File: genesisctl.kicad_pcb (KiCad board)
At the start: 2 copper layers, 12 parts, among them J1 Conn_02x05_Odd_Even, J2 Screw_Terminal_01x02, J3 Screw_Terminal_01x04, J4 Screw_Terminal_01x04, U1 NE555, U2 74LS374, U3 74LS74, U4 74LS374

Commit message: added gerber files
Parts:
- C1, C2: value 3.3uF -> 0.22uF
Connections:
- U4 pad 2: /left_out -> /right_out
- U4 pad 3: /gnd_left -> /gnd_right
- U4 pad 4: /gnd_right -> /gnd_left
- U4 pad 5: /right_out -> /left_out
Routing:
- net /select: track 0.00 -> 90.6 mm
- net /btna_out: track 0.00 -> 51.9 mm
- net Net-(U2-Pad11): track 0.00 -> 42.5 mm
- net /start_btnc: track 0.00 -> 34.0 mm
- net /right_out: track 0.00 -> 31.7 mm
- net /btna_btnb: track 0.00 -> 31.4 mm
- net btnb_out: track 0.00 -> 31.3 mm
- net Net-(C2-Pad1): track 0.00 -> 27.6 mm
- net /down: track 0.00 -> 26.3 mm
- net /up: track 0.00 -> 26.2 mm
- net btnc_out: track 0.00 -> 23.6 mm
- net /left_out: track 0.00 -> 23.2 mm
- net /start_out: track 0.00 -> 21.5 mm
- net GND: track 0.00 -> 17.7 mm, vias 0 -> 4
- net Net-(C1-Pad1): track 0.00 -> 16.1 mm
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- added copper zone on B.Cu, net +5V
- added copper zone on F.Cu, net GND
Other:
- board outline added: 48.3 x 63.5 mm
- board text added: "+5V"
- board text added: "A"
- board text added: "B"
- board text added: "C"
- board text added: "Down"
- board text added: "GND"
- board text added: "Genesis Jamma v1.0 2021 Sean Kasun"
- board text added: "Left"
- board text added: "Pin1"
- board text added: "Right"
- board text added: "Start"
- board text added: "Up"

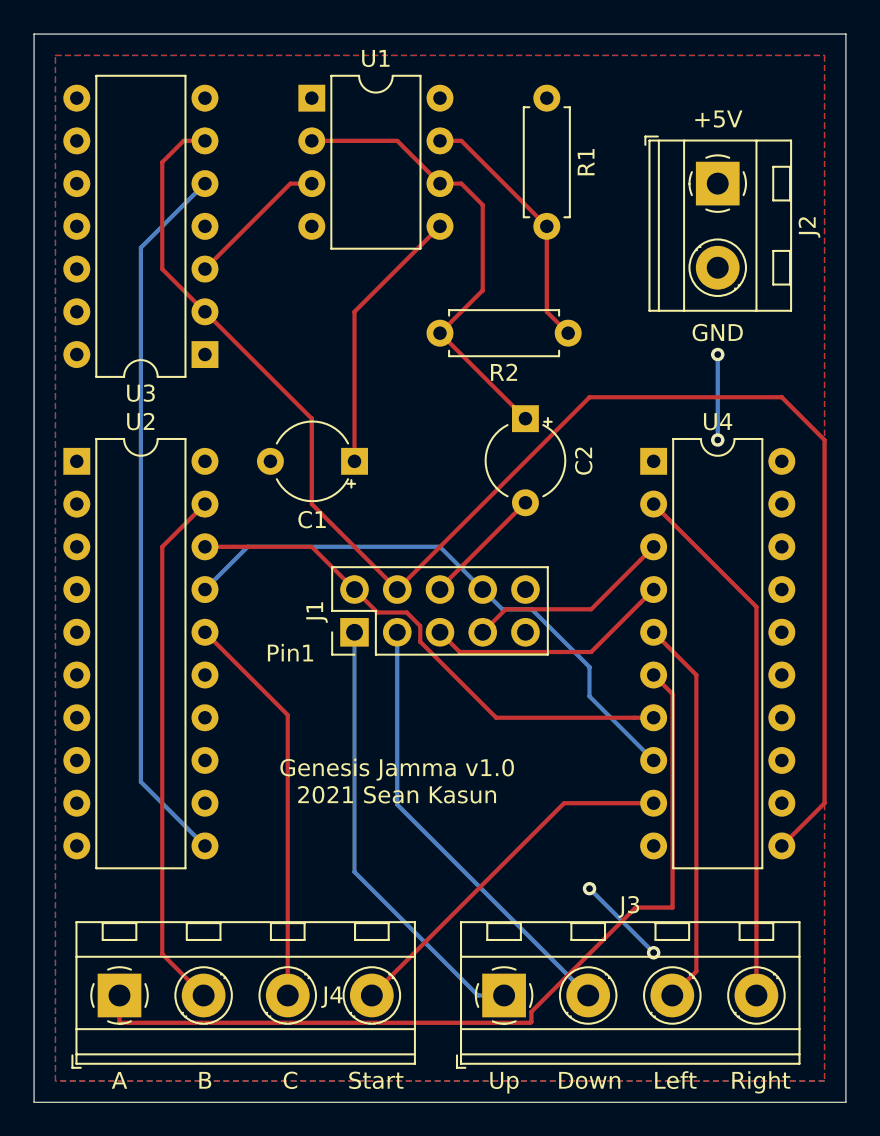
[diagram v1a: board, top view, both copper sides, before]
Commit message: fixed reversed left/right
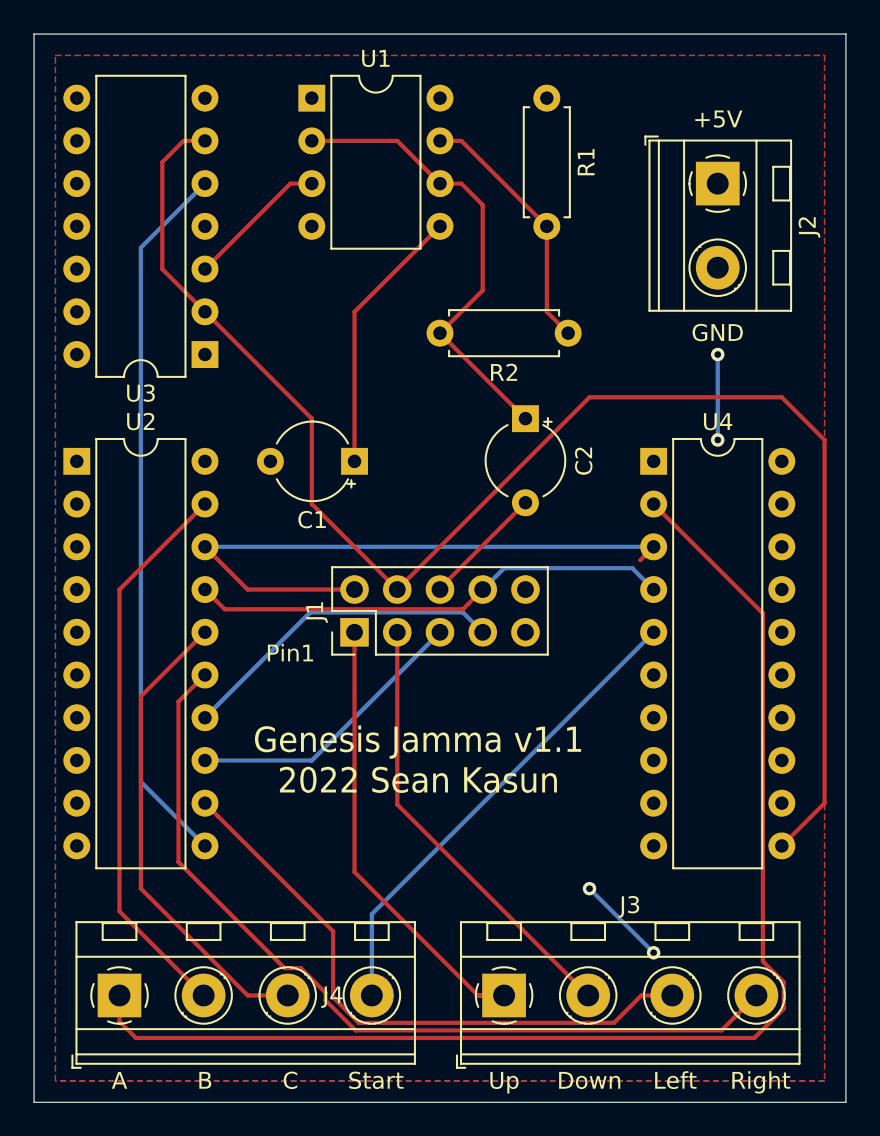
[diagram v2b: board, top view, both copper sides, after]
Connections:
- J3 pad 3: /left_out -> left_out
- J3 pad 4: /right_out -> right_out
- J4 pad 1: /btna_out -> Net-(J4-Pad1)
- J4 pad 4: /start_out -> /btna_out
- U2 pad 12: (no net) -> left_out
- U2 pad 13: (no net) -> /gnd_left
- U2 pad 14: (no net) -> /gnd_right
- U2 pad 15: (no net) -> right_out
- U4 pad 2: /right_out -> Net-(J4-Pad1)
- U4 pad 3: /gnd_right -> /btna_btnb
- U4 pad 4: /gnd_left -> /start_btnc
- U4 pad 5: /left_out -> /btna_out
- U4 pad 6: /btna_out -> (no net)
- U4 pad 7: /btna_btnb -> (no net)
- U4 pad 8: /start_btnc -> (no net)
- U4 pad 9: /start_out -> (no net)
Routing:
- net Net-(J4-Pad1): track 0.00 -> 75.4 mm
- net right_out: track 0.00 -> 51.4 mm
- net left_out: track 0.00 -> 36.2 mm
- net /right_out: track 31.7 -> 0.00 mm
- net /btna_out: track 51.9 -> 28.5 mm
- net /left_out: track 23.2 -> 0.00 mm
- net /start_out: track 21.5 -> 0.00 mm
- net /gnd_right: track 12.3 -> 19.6 mm
- net /btna_btnb: track 31.4 -> 37.7 mm
- net /start_btnc: track 34.0 -> 28.7 mm
- net btnc_out: track 23.6 -> 28.2 mm
- net /gnd_left: track 14.7 -> 17.1 mm
- net btnb_out: track 31.3 -> 33.4 mm
- net /up: track 26.2 -> 27.7 mm
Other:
- board text added: "Genesis Jamma v1.1 2022 Sean Kasun"
- board text removed: "Genesis Jamma v1.0 2021 Sean Kasun"
